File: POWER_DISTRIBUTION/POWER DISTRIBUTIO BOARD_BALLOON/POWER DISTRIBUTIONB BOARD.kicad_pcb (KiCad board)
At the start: 4 copper layers, 94.5 x 55 mm, 98 parts, among them IC3 TPS1HB08BQPWPRQ1, IC4 TPS1HB08BQPWPRQ1, IC8 INA232AIDDFR, IC9 TCAN1044VDDFR, J10 Conn_01x02, J11 Conn_01x02, J28 Conn_01x06, J29 Conn_01x02, J30 Conn_01x02, J31 Conn_01x02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

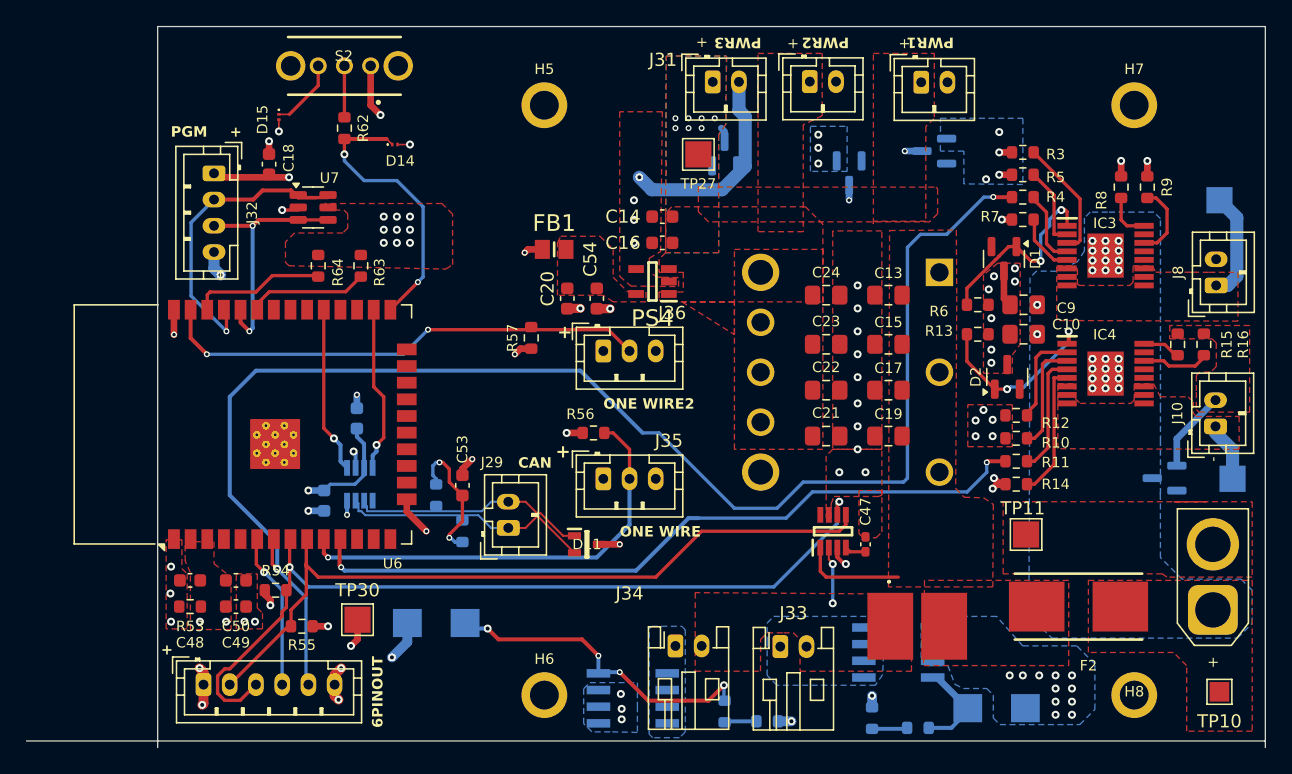
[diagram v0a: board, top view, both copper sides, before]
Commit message: edited the BAT to SSC diode
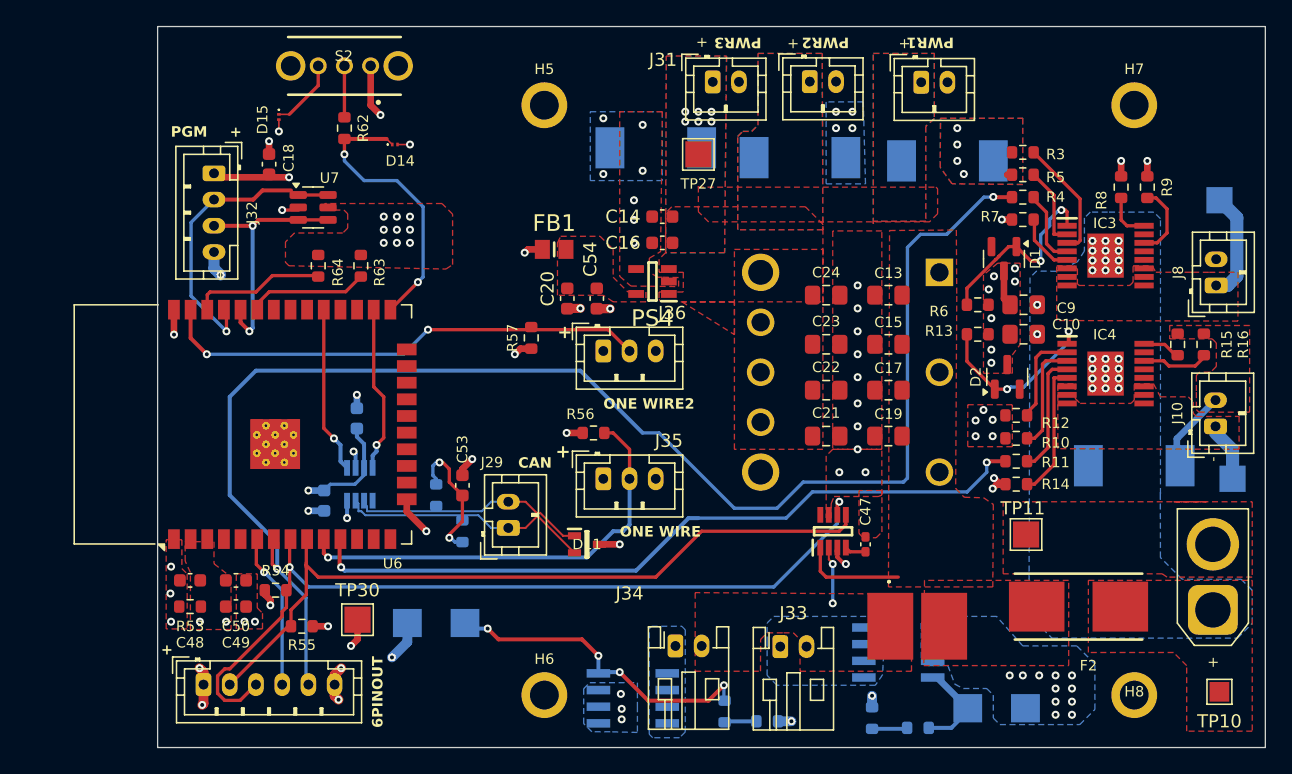
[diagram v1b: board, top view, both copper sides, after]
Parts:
- removed D12, D13: BAS21, Package_TO_SOT_SMD:SOT-23
- added D7: SSC53L-E3_57T, SamacSys_COMMS:DIOM7959X262N, B.Cu at (188.5, 105.5)
- added D9: SSC53L-E3_57T, SamacSys_COMMS:DIOM7959X262N, B.Cu at (152.0, 81.2)
- D10, D8: value BAS21 -> SSC53L-E3_57T; footprint Package_TO_SOT_SMD:SOT-23 -> SamacSys_COMMS:DIOM7959X262N
- moved D8 29.3 mm to (174.2, 82.2), turned to 0 degrees
- moved D10 3.93 mm to (163.0, 82.0), turned to 0 degrees
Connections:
- D10 pad 1: GND -> +5V0
- D10 pad 2: unconnected-(D10-NC-Pad2) -> GND
- D8 pad 1: GND -> +5V0
- D8 pad 2: unconnected-(D8-NC-Pad2) -> GND
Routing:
- net GND: track 66.5 -> 49.3 mm, vias 79 -> 83
- net +5V0: track 2.79 -> 0.00 mm, vias 9 -> 6
- net PGM_RX: track 24.9 -> 22.5 mm
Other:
- board size 94.5 x 55 mm -> 84.5 x 55 mm
